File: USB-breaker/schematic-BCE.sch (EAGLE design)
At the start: 27 parts, among them K1 G6K-2P, K2 G6K-2P, T1 2PA733, T2 2SC945, X1 PN61729-S, X2 PN87520-S, X3 10104110, X4 UX60SC-MB-5ST

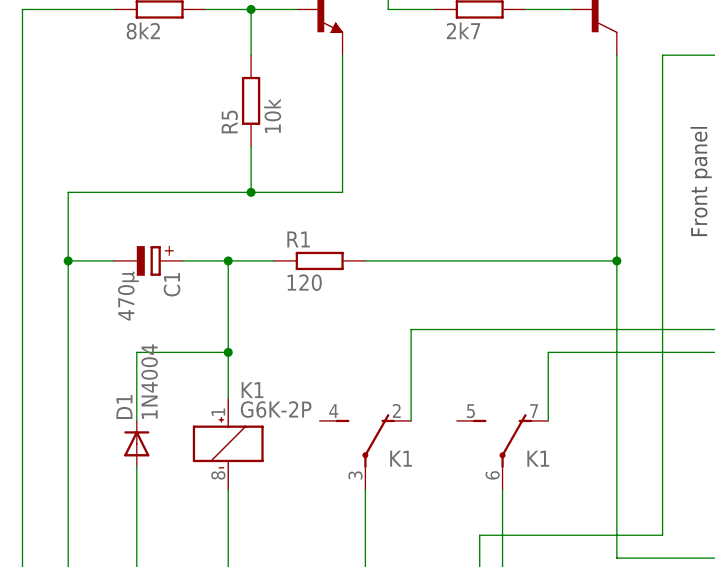
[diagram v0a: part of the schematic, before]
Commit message: Value of R1 changed from 120 Ω to 100 Ω. Otherwise the voltage for relay K1 is too low.
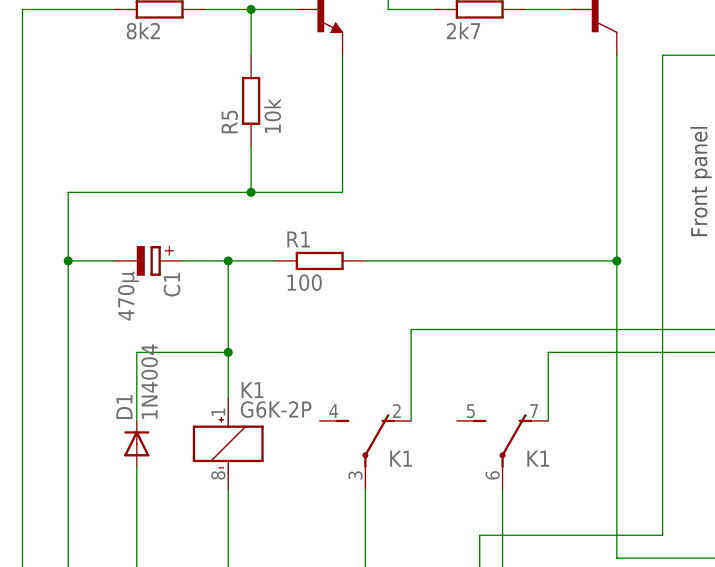
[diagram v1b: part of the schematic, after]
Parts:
- R1: value 120 -> 100
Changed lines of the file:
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@@
 <parts>
 <part name="FRAME1" library="frames" deviceset="DINA5_L" device=""/>
-<part name="R1" library="resistor" deviceset="R-EU_" device="0207/10" value="120"/>
+<part name="R1" library="resistor" deviceset="R-EU_" device="0207/10" value="100"/>
 <part name="C1" library="resistor" deviceset="CPOL-EU" device="E3.5-8" value="470µ"/>
 <part name="D1" library="diode" deviceset="1N4004" device=""/>

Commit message: T1 is now used from another library. BCE was wrong, ECB is the right package.
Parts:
- T1: device transistor:BC369-PNP-TO92-BCE -> mibe:2PA733
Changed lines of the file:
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@@
 <part name="U$4" library="mibe" deviceset="EXTERNAL_SWITCH" device=""/>
 <part name="JP1" library="pinhead" deviceset="PINHD-1X7" device="/90"/>
-<part name="T1" library="transistor" deviceset="*-PNP-" device="TO92-BCE" technology="BC369" value="2PA733"/>
+<part name="T1" library="mibe" deviceset="2PA733" device="" value="2PA733"/>
 <part name="R3" library="resistor" deviceset="R-EU_" device="0207/10" value="2k7"/>
 <part name="T2" library="transistor" deviceset="2SC945" device="" value="2SC945"/>
